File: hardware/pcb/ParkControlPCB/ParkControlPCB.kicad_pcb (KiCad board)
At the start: 2 copper layers, 19 parts, among them J1 Prog, J2 PWR, J3 LED1, J4 LED2, J5 US1, J6 US2, J7 US3, U1 LM1117-3.3, U2 ESP-12F, U3 TXS0108EPW

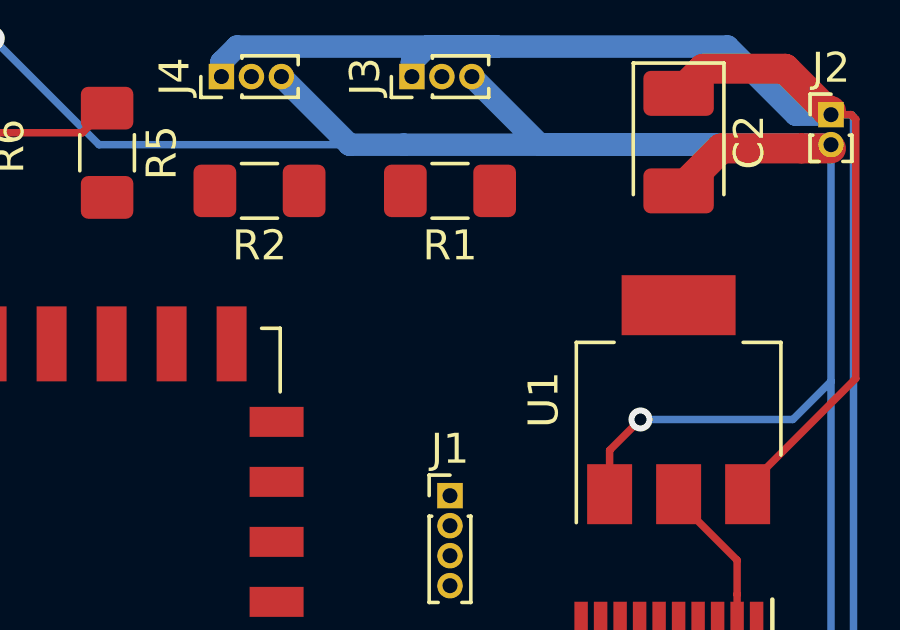
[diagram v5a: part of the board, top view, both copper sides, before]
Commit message: Fix missing pull-down on txs0108 OE pin
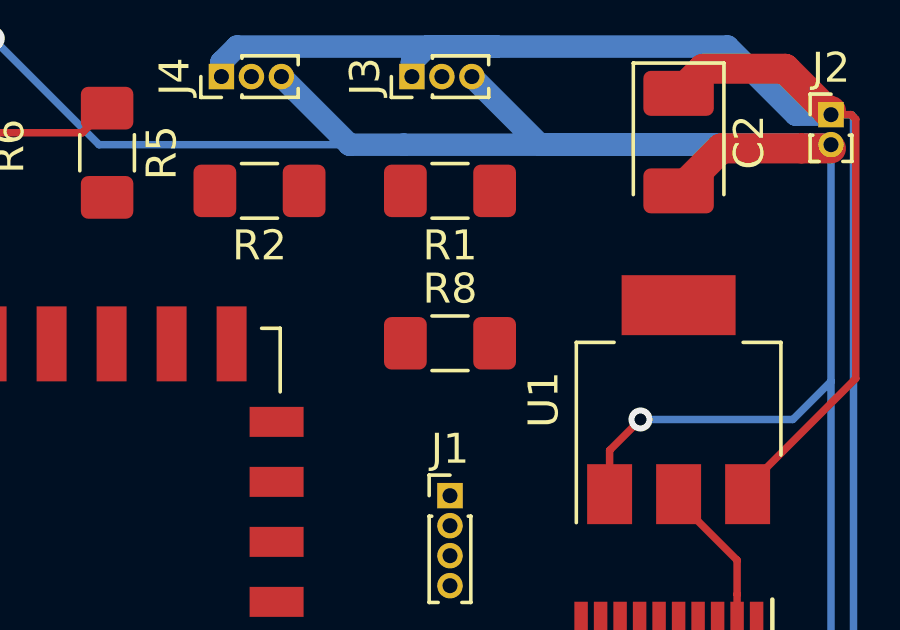
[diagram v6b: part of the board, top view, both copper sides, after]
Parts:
- added R8: 10K, Resistor_SMD:R_1206_3216Metric_Pad1.42x1.75mm_HandSolder, F.Cu at (129.5, 86.4)
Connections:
- U2 pad 11: /OE -> Net-(U2-Pad11)
- U2 pad 4: /US_E_3 -> /OE
- U2 pad 5: /US_T_3 -> Net-(U2-Pad5)
- U3 pad 12: /US_E_3_5V -> Net-(U3-Pad12)
- U3 pad 13: /US_T_3_5V -> Net-(U3-Pad13)
- U3 pad 8: /US_T_3 -> Net-(U3-Pad8)
- U3 pad 9: /US_E_3 -> Net-(U3-Pad9)
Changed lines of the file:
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@@
     (tracks 109)
     (zones 0)
-    (modules 19)
-    (nets 34)
+    (modules 20)
+    (nets 38)
   )
   (page A4)
@@
   (net 29 /US_E_3_5V)
   (net 30 /US_T_3_5V)
-  (net 31 /US_T_3)
-  (net 32 /US_E_3)
-  (net 33 /OE)
+  (net 31 /OE)
+  (net 32 "Net-(U2-Pad11)")
+  (net 33 "Net-(U2-Pad5)")
+  (net 34 "Net-(U3-Pad13)")
+  (net 35 "Net-(U3-Pad12)")
+  (net 36 "Net-(U3-Pad9)")
+  (net 37 "Net-(U3-Pad8)")
   (net_class Default "This is the default net class."
     (clearance 0.2)
@@
     (add_net /US_E_2)
     (add_net /US_E_2_5V)
-    (add_net /US_E_3)
     (add_net /US_E_3_5V)
     (add_net /US_T_1)
@@
     (add_net /US_T_2)
     (add_net /US_T_2_5V)
-    (add_net /US_T_3)
     (add_net /US_T_3_5V)
     (add_net GND)
@@
     (add_net "Net-(R6-Pad2)")
     (add_net "Net-(R7-Pad1)")
+    (add_net "Net-(U2-Pad11)")
     (add_net "Net-(U2-Pad12)")
     (add_net "Net-(U2-Pad2)")
+    (add_net "Net-(U2-Pad5)")
+    (add_net "Net-(U3-Pad12)")
+    (add_net "Net-(U3-Pad13)")
+    (add_net "Net-(U3-Pad8)")
+    (add_net "Net-(U3-Pad9)")
     (add_net VCC)
   )
@@
     (uvia_dia 0.3)
     (uvia_drill 0.1)
+  )
+  (module Resistor_SMD:R_1206_3216Metric_Pad1.42x1.75mm_HandSolder (layer F.Cu)
+    (at 129.54 86.36)
+    (descr "Resistor SMD 1206 (3216 Metric), square (rectangular) end terminal, IPC_7351 nominal with elongated pad for handsoldering. (Body size source: http://www.tortai-tech.com/upload/download/2011102023233369053.pdf), generated with kicad-footprint-generator")
+    (tags "resistor handsolder")
+    (attr smd)
+    (fp_text reference R8 (at 0 -1.82) (layer F.SilkS)
+      (effects (font (size 1 1) (thickness 0.15)))
+    )
+    (fp_text value 10K (at 0 1.82) (layer F.Fab)
+      (effects (font (size 1 1) (thickness 0.15)))
+    )
+    (fp_text user %R (at 0 0) (layer F.Fab)
+      (effects (font (size 0.8 0.8) (thickness 0.12)))
+    )
+    (fp_line (start 2.45 1.12) (end -2.45 1.12) (layer F.CrtYd) (width 0.05))
+    (fp_line (start 2.45 -1.12) (end 2.45 1.12) (layer F.CrtYd) (width 0.05))
+    (fp_line (start -2.45 -1.12) (end 2.45 -1.12) (layer F.CrtYd) (width 0.05))
+    (fp_line (start -2.45 1.12) (end -2.45 -1.12) (layer F.CrtYd) (width 0.05))
+    (fp_line (start -0.602064 0.91) (end 0.602064 0.91) (layer F.SilkS) (width 0.12))
+    (fp_line (start -0.602064 -0.91) (end 0.602064 -0.91) (layer F.SilkS) (width 0.12))
+    (fp_line (start 1.6 0.8) (end -1.6 0.8) (layer F.Fab) (width 0.1))
+    (fp_line (start 1.6 -0.8) (end 1.6 0.8) (layer F.Fab) (width 0.1))
+    (fp_line (start -1.6 -0.8) (end 1.6 -0.8) (layer F.Fab) (width 0.1))
+    (fp_line (start -1.6 0.8) (end -1.6 -0.8) (layer F.Fab) (width 0.1))
+    (pad 2 smd roundrect (at 1.4875 0) (size 1.425 1.75) (layers F.Cu F.Paste F.Mask) (roundrect_rratio 0.175439)
+      (net 4 GND))
+    (pad 1 smd roundrect (at -1.4875 0) (size 1.425 1.75) (layers F.Cu F.Paste F.Mask) (roundrect_rratio 0.175439)
+      (net 31 /OE))
+    (model ${KISYS3DMOD}/Resistor_SMD.3dshapes/R_1206_3216Metric.wrl
+      (at (xyz 0 0 0))
+      (scale (xyz 1 1 1))
+      (rotate (xyz 0 0 0))
+    )
   )
   (module Connector_PinHeader_1.00mm:PinHeader_1x02_P1.00mm_Vertical (layer F.Cu)
@@
       (net 28 /US_E_2_5V))
     (pad 13 smd rect (at 2.95 1.625 270) (size 1.45 0.45) (layers F.Cu F.Paste F.Mask)
-      (net 30 /US_T_3_5V))
+      (net 34 "Net-(U3-Pad13)"))
     (pad 12 smd rect (at 2.95 2.275 270) (size 1.45 0.45) (layers F.Cu F.Paste F.Mask)
-      (net 29 /US_E_3_5V))
+      (net 35 "Net-(U3-Pad12)"))
     (pad 11 smd rect (at 2.95 2.925 270) (size 1.45 0.45) (layers F.Cu F.Paste F.Mask)
       (net 4 GND))
     (pad 10 smd rect (at -2.95 2.925 270) (size 1.45 0.45) (layers F.Cu F.Paste F.Mask)
-      (net 33 /OE))
+      (net 31 /OE))
     (pad 9 smd rect (at -2.95 2.275 270) (size 1.45 0.45) (layers F.Cu F.Paste F.Mask)
-      (net 32 /US_E_3))
+      (net 36 "Net-(U3-Pad9)"))
     (pad 8 smd rect (at -2.95 1.625 270) (size 1.45 0.45) (layers F.Cu F.Paste F.Mask)
-      (net 31 /US_T_3))
+      (net 37 "Net-(U3-Pad8)"))
     (pad 7 smd rect (at -2.95 0.975 270) (size 1.45 0.45) (layers F.Cu F.Paste F.Mask)
       (net 23 /US_E_2))
@@
       (net 2 "Net-(U2-Pad12)"))
     (pad 11 smd rect (at -1 12 90) (size 1 1.8) (layers F.Cu F.Paste F.Mask)
-      (net 33 /OE))
+      (net 32 "Net-(U2-Pad11)"))
     (pad 10 smd rect (at -3 12 90) (size 1 1.8) (layers F.Cu F.Paste F.Mask)
       (net 8 /MISO))
@@
       (net 24 /US_T_2))
     (pad 5 smd rect (at -7.6 4.5 90) (size 2.5 1) (layers F.Cu F.Paste F.Mask)
-      (net 31 /US_T_3))
+      (net 33 "Net-(U2-Pad5)"))
     (pad 4 smd rect (at -7.6 2.5 90) (size 2.5 1) (layers F.Cu F.Paste F.Mask)
-      (net 32 /US_E_3))
+      (net 31 /OE))
     (pad 3 smd rect (at -7.6 0.5 90) (size 2.5 1) (layers F.Cu F.Paste F.Mask)
       (net 20 "Net-(R7-Pad1)"))
